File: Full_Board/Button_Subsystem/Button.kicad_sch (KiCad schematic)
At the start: 6 parts

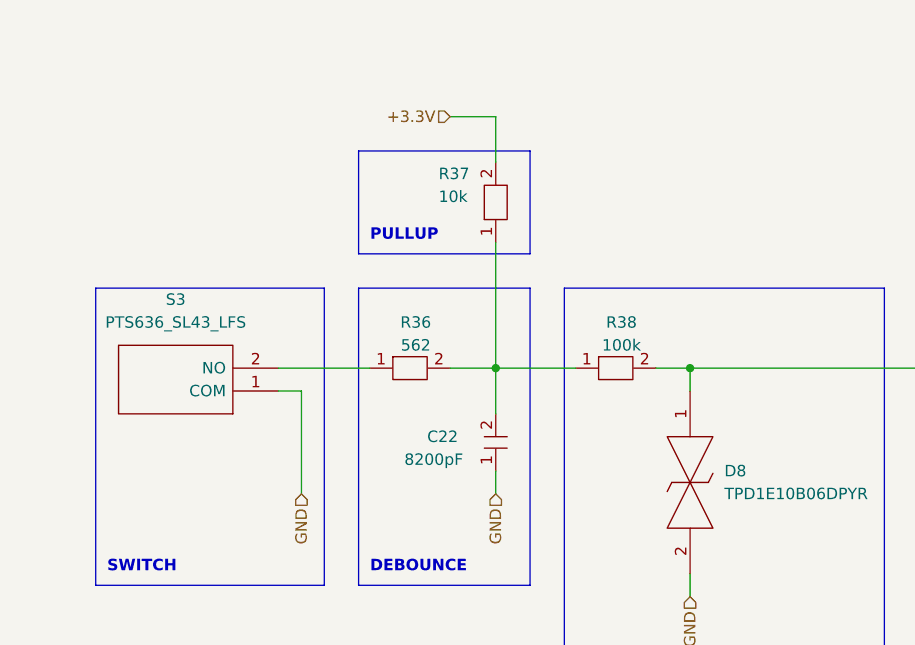
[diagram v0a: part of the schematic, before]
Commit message: Added 5V power supply
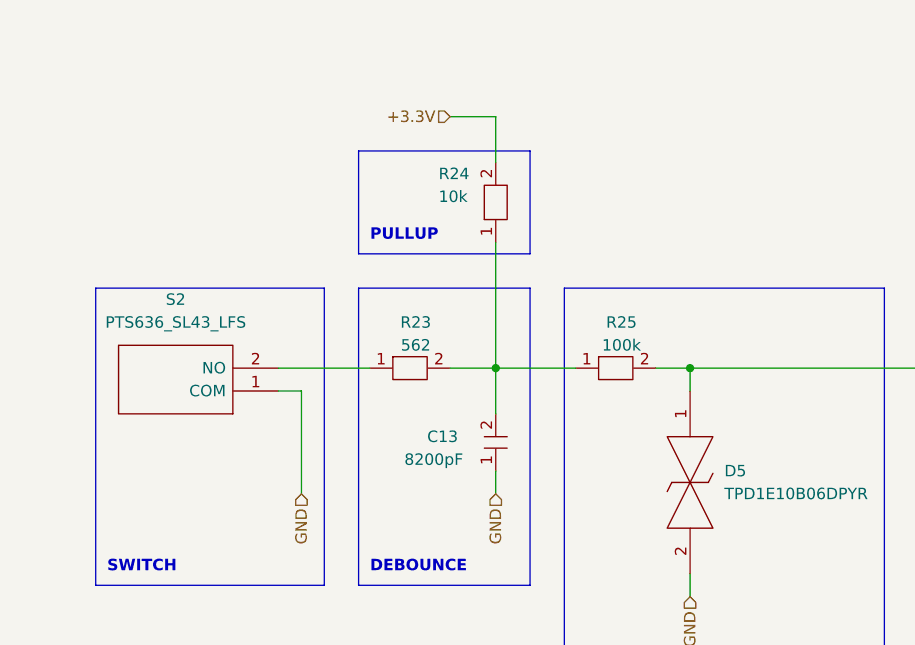
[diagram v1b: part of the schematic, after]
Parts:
- renumbered C22 to C13, D8 to D5, R36 to R23, R37 to R24, R38 to R25, S3 to S2
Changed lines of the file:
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@@
     (effects (font (size 1.27 1.27)) (justify right))
   )
-  (symbol (lib_id "CR0402-FX-5620GLF:CR0402-FX-5620GLF") (at 123.19 96.52 0) (unit 1)
+  (symbol (lib_id "CR0402-FX-5620GLF:CR0402-FX-5620GLF") (at 123.19 96.52 0)
     (in_bom yes) (on_board yes)
-    (property "Reference" "R36" (id 0) (at 128.27 91.44 0))
+    (property "Reference" "R23" (id 0) (at 128.27 91.44 0))
     (property "Value" "562" (id 1) (at 128.27 93.98 0))
     (property "Footprint" "CR0402-FX-5620GLF:RESC1005X40N" (id 2) (at 137.16 95.25 0)
@@
     (pin "2")
   )
-  (symbol (lib_id "TPD1E10B06DPYR:TPD1E10B06DPYR") (at 158.75 99.06 270) (unit 1)
+  (symbol (lib_id "TPD1E10B06DPYR:TPD1E10B06DPYR") (at 158.75 99.06 270)
     (in_bom yes) (on_board yes)
-    (property "Reference" "D8" (id 0) (at 162.56 107.95 90)
+    (property "Reference" "D5" (id 0) (at 162.56 107.95 90)
       (effects (font (size 1.27 1.27)) (justify left))
     )
@@
     (pin "2")
   )
-  (symbol (lib_id "RCV2512100KFKEGAT:RCV2512100KFKEGAT") (at 146.05 96.52 0) (unit 1)
+  (symbol (lib_id "RCV2512100KFKEGAT:RCV2512100KFKEGAT") (at 146.05 96.52 0)
     (in_bom yes) (on_board yes)
-    (property "Reference" "R38" (id 0) (at 151.13 91.44 0))
+    (property "Reference" "R25" (id 0) (at 151.13 91.44 0))
     (property "Value" "100k" (id 1) (at 151.13 93.98 0))
     (property "Footprint" "RCV2512100KFKEGAT:RESC6332X70N" (id 2) (at 160.02 95.25 0)
@@
     (pin "2")
   )
-  (symbol (lib_id "CRMA1210AF10K0DKEF:10k") (at 137.16 82.55 90) (unit 1)
+  (symbol (lib_id "CRMA1210AF10K0DKEF:10k") (at 137.16 82.55 90)
     (in_bom yes) (on_board yes)
-    (property "Reference" "R37" (id 0) (at 130.81 74.93 90)
+    (property "Reference" "R24" (id 0) (at 130.81 74.93 90)
       (effects (font (size 1.27 1.27)) (justify right))
     )
@@
     (pin "2")
   )
-  (symbol (lib_id "PTS636_SL43_LFS:PTS636_SL43_LFS") (at 113.03 99.06 180) (unit 1)
+  (symbol (lib_id "PTS636_SL43_LFS:PTS636_SL43_LFS") (at 113.03 99.06 180)
     (in_bom yes) (on_board yes) (fields_autoplaced)
-    (property "Reference" "S3" (id 0) (at 101.6 88.9 0))
+    (property "Reference" "S2" (id 0) (at 101.6 88.9 0))
     (property "Value" "PTS636_SL43_LFS" (id 1) (at 101.6 91.44 0))
     (property "Footprint" "PTS636_SL43_LFS:PTS636SL43LFS" (id 2) (at 93.98 101.6 0)
@@
     (pin "2")
   )
-  (symbol (lib_id "C1210C822K2RACAUTO:8200pF") (at 137.16 107.95 90) (unit 1)
+  (symbol (lib_id "C1210C822K2RACAUTO:8200pF") (at 137.16 107.95 90)
     (in_bom yes) (on_board yes)
-    (property "Reference" "C22" (id 0) (at 129.54 104.14 90)
+    (property "Reference" "C13" (id 0) (at 129.54 104.14 90)
       (effects (font (size 1.27 1.27)) (justify right))
     )

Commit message: Added extra bypass caps to the power supply
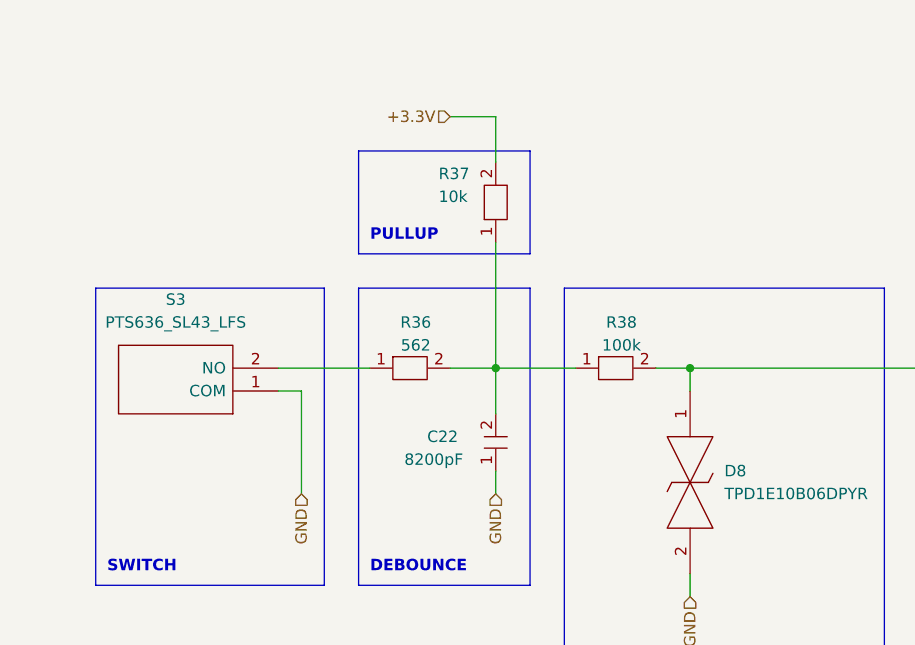
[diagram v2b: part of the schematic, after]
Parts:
- renumbered C13 to C22, D5 to D8, R23 to R36, R24 to R37, R25 to R38, S2 to S3
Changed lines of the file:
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@@
   (symbol (lib_id "CR0402-FX-5620GLF:CR0402-FX-5620GLF") (at 123.19 96.52 0)
     (in_bom yes) (on_board yes)
-    (property "Reference" "R23" (id 0) (at 128.27 91.44 0))
+    (property "Reference" "R36" (id 0) (at 128.27 91.44 0))
     (property "Value" "562" (id 1) (at 128.27 93.98 0))
     (property "Footprint" "CR0402-FX-5620GLF:RESC1005X40N" (id 2) (at 137.16 95.25 0)
@@
   (symbol (lib_id "TPD1E10B06DPYR:TPD1E10B06DPYR") (at 158.75 99.06 270)
     (in_bom yes) (on_board yes)
-    (property "Reference" "D5" (id 0) (at 162.56 107.95 90)
+    (property "Reference" "D8" (id 0) (at 162.56 107.95 90)
       (effects (font (size 1.27 1.27)) (justify left))
     )
@@
   (symbol (lib_id "RCV2512100KFKEGAT:RCV2512100KFKEGAT") (at 146.05 96.52 0)
     (in_bom yes) (on_board yes)
-    (property "Reference" "R25" (id 0) (at 151.13 91.44 0))
+    (property "Reference" "R38" (id 0) (at 151.13 91.44 0))
     (property "Value" "100k" (id 1) (at 151.13 93.98 0))
     (property "Footprint" "RCV2512100KFKEGAT:RESC6332X70N" (id 2) (at 160.02 95.25 0)
@@
   (symbol (lib_id "CRMA1210AF10K0DKEF:10k") (at 137.16 82.55 90)
     (in_bom yes) (on_board yes)
-    (property "Reference" "R24" (id 0) (at 130.81 74.93 90)
+    (property "Reference" "R37" (id 0) (at 130.81 74.93 90)
       (effects (font (size 1.27 1.27)) (justify right))
     )
@@
   (symbol (lib_id "PTS636_SL43_LFS:PTS636_SL43_LFS") (at 113.03 99.06 180)
     (in_bom yes) (on_board yes) (fields_autoplaced)
-    (property "Reference" "S2" (id 0) (at 101.6 88.9 0))
+    (property "Reference" "S3" (id 0) (at 101.6 88.9 0))
     (property "Value" "PTS636_SL43_LFS" (id 1) (at 101.6 91.44 0))
     (property "Footprint" "PTS636_SL43_LFS:PTS636SL43LFS" (id 2) (at 93.98 101.6 0)
@@
   (symbol (lib_id "C1210C822K2RACAUTO:8200pF") (at 137.16 107.95 90)
     (in_bom yes) (on_board yes)
-    (property "Reference" "C13" (id 0) (at 129.54 104.14 90)
+    (property "Reference" "C22" (id 0) (at 129.54 104.14 90)
       (effects (font (size 1.27 1.27)) (justify right))
     )

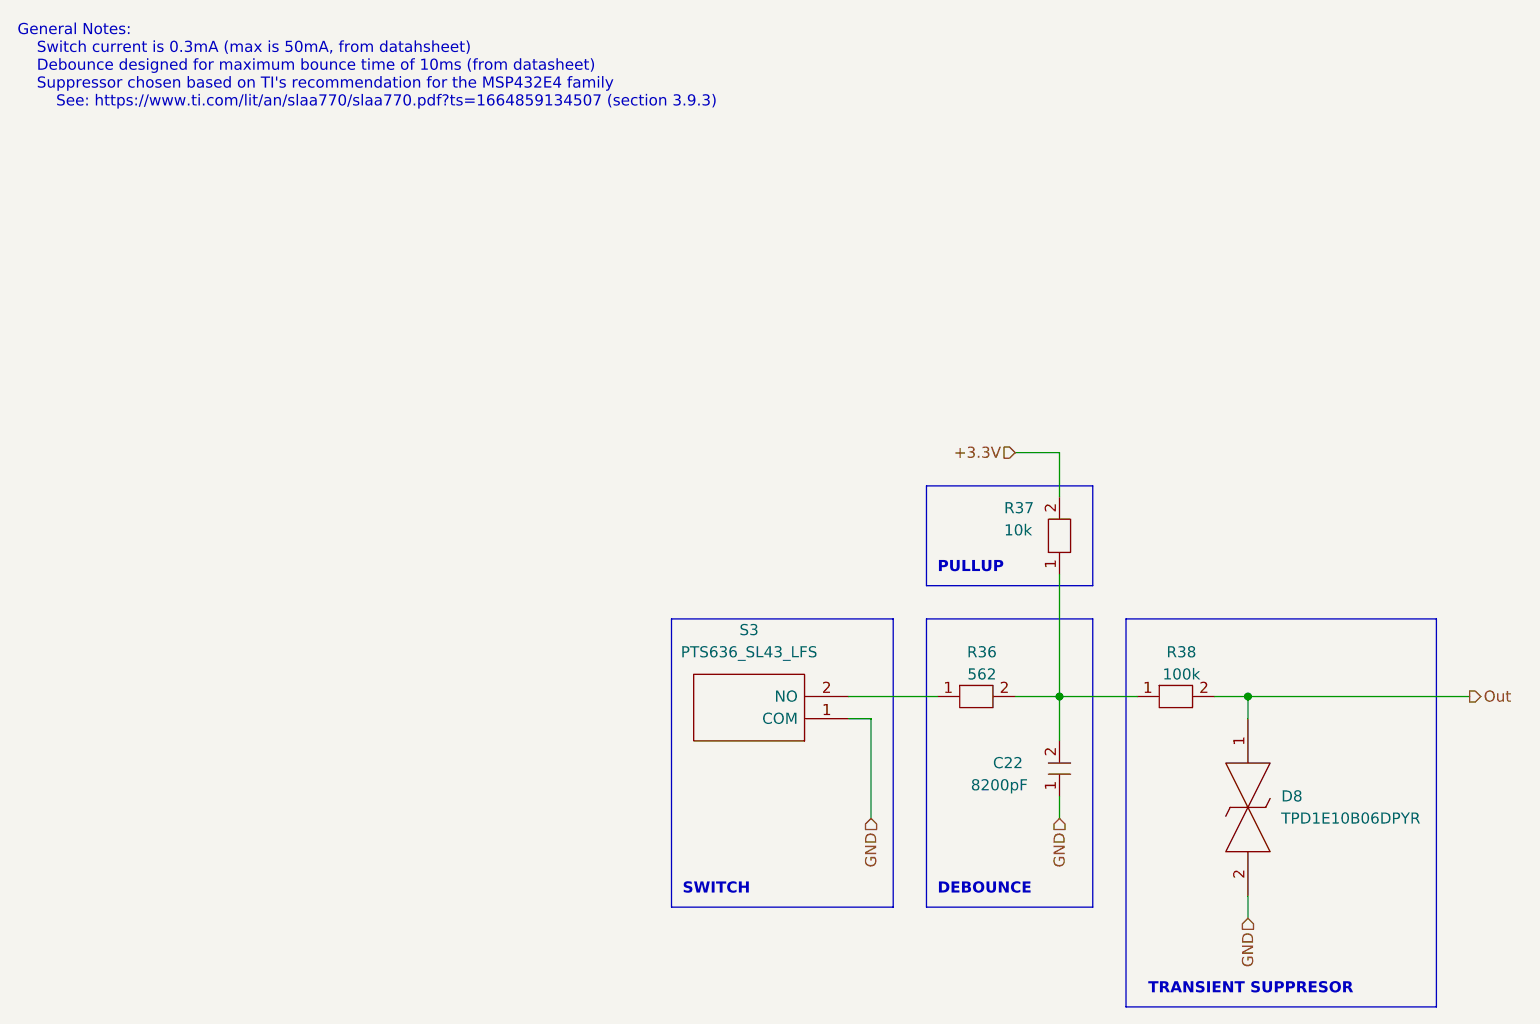
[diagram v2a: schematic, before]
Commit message: Merge Eli and Gabi files. Remove unecessary ECAD remnants. Update stepper components post-part order
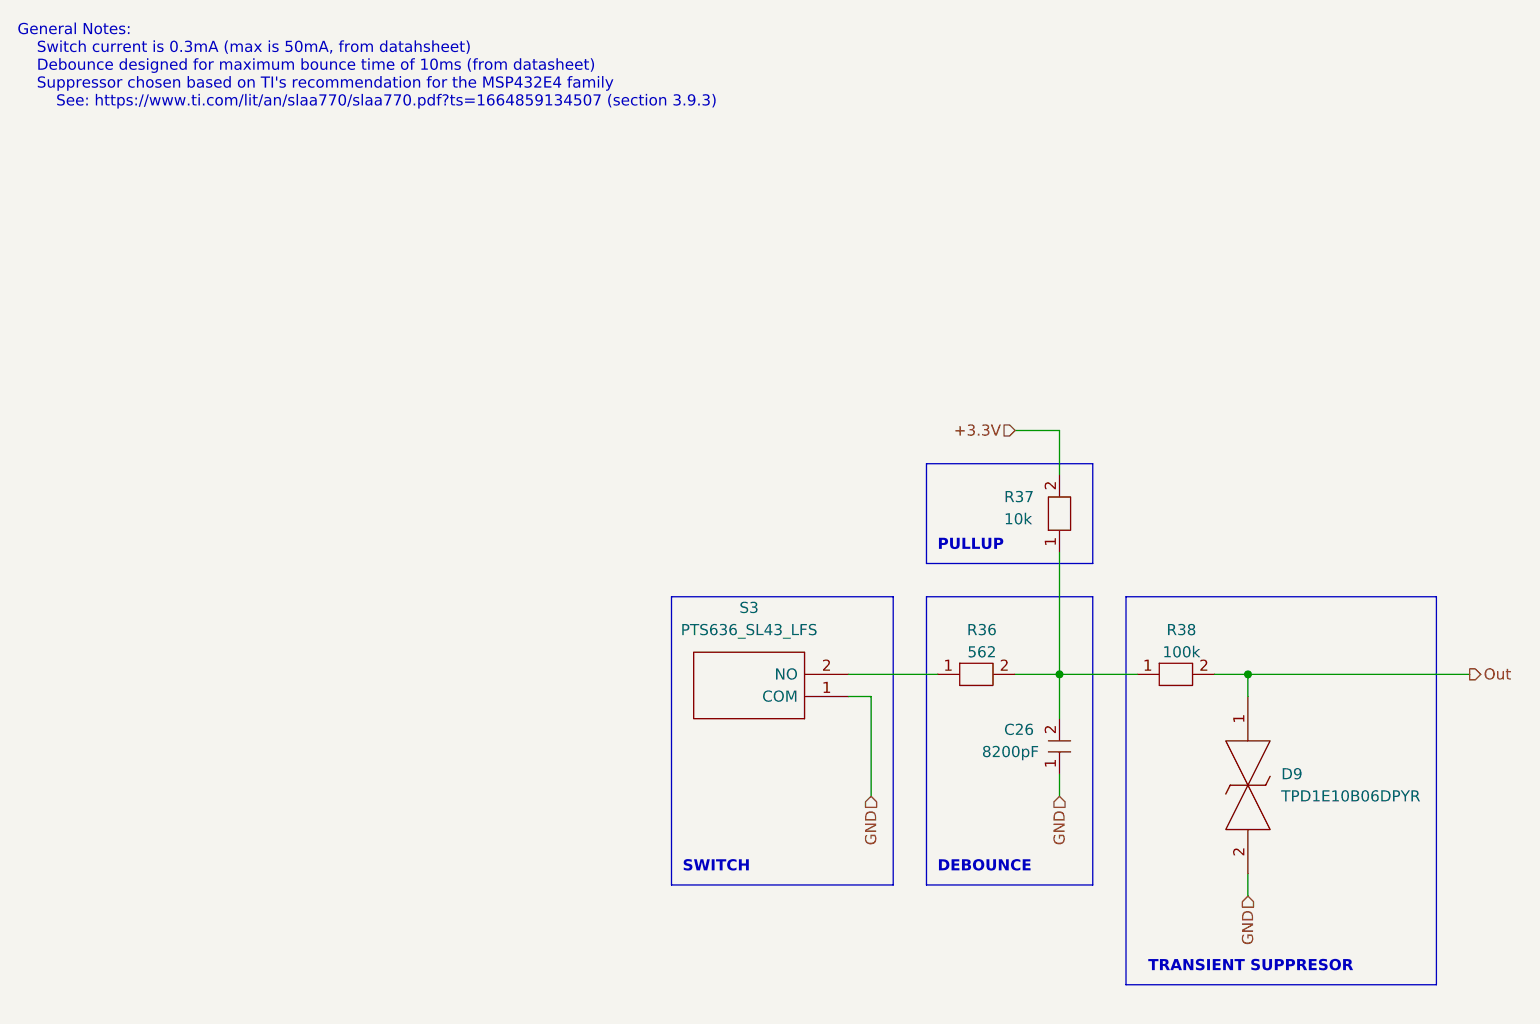
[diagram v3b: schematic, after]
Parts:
- removed C22: 8200pF, C1210C822K2RACAUTO:CAPC3225X88N, symbol C1210C822K2RACAUTO:8200pF
- removed D8: TPD1E10B06DPYR, TPD1E10B06DPYR:TPD1E10B06DPYR, symbol TPD1E10B06DPYR:TPD1E10B06DPYR
- removed R37: 10k, CRMA1210AF10K0DKEF:RESC3225X74N, symbol CRMA1210AF10K0DKEF:10k
- added C26: 8200pF, C1210C822K2RACAUTO:CAPC3225X88N, symbol C1210C822K2RACAUTO:C1210C822K2RACAUTO
- added D9: TPD1E10B06DPYR, TPD1E10B06DPYR:TPD1E10B06DPYR, symbol TPD1E10B06DPYR:TPD1E10B06DPYR
- added R37: 10k, RESC3225X74N, symbol RMCF1206FT10K0:10k
- R36: Mouse link (none) -> https://www.mouser.com/ProductDetail/Bourns/CR0402-FX-5620G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; Mouser link https://www.mouser.com/ProductDetail/Bourns/CR0402-FX-5620G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 -> (none)
- S3: Mouser link  (none) -> https://www.mouser.com/ProductDetail/CK/PTS636-SL43-LFS?qs=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
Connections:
- net +3.3V: now also R37.2
- net GND: now also C26.1, D9.2
- net Out: now also D9.1
- net at R36.2, R38.1: now also C26.2, R37.1

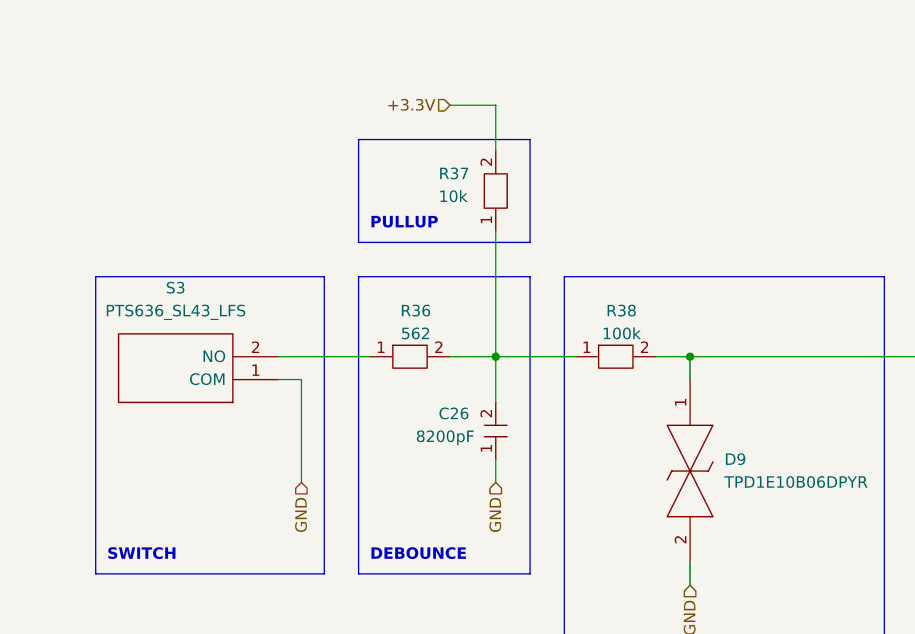
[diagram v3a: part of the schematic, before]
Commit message: Added a fuse and fixed ERC
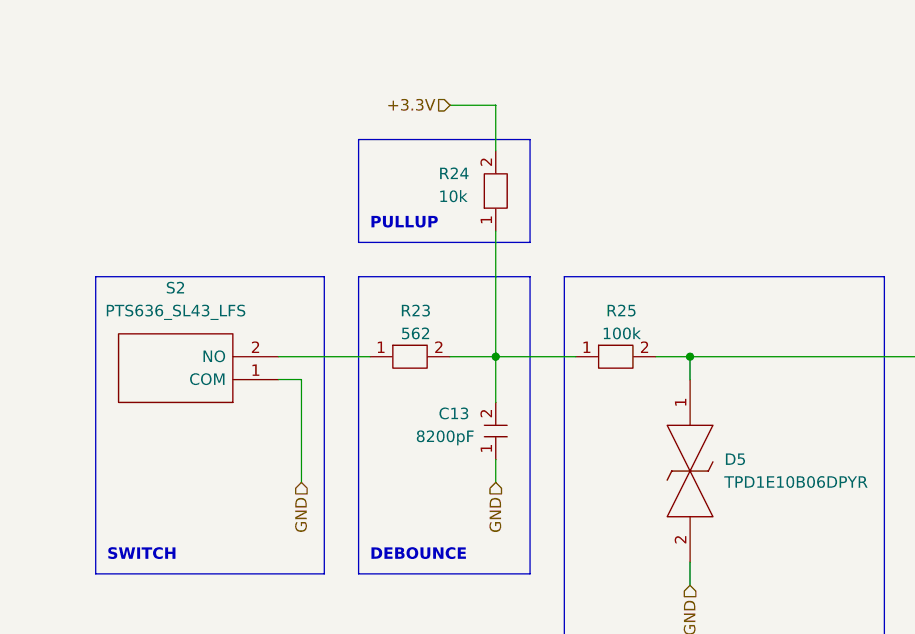
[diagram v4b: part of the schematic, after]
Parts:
- renumbered C26 to C13, D9 to D5, R36 to R23, R37 to R24, R38 to R25, S3 to S2
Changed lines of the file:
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@@
     (effects (font (size 1.27 1.27)) (justify right))
   )
-  (symbol (lib_id "RMCF1206FT10K0:10k") (at 137.16 80.01 90) (unit 1)
+  (symbol (lib_id "RMCF1206FT10K0:10k") (at 137.16 80.01 90)
     (in_bom yes) (on_board yes)
-    (property "Reference" "R37" (id 0) (at 130.81 73.66 90)
+    (property "Reference" "R24" (id 0) (at 130.81 73.66 90)
       (effects (font (size 1.27 1.27)) (justify right))
     )
@@
     (pin "2")
   )
-  (symbol (lib_id "C1210C822K2RACAUTO:C1210C822K2RACAUTO") (at 137.16 105.41 90) (unit 1)
+  (symbol (lib_id "C1210C822K2RACAUTO:C1210C822K2RACAUTO") (at 137.16 105.41 90)
     (in_bom yes) (on_board yes)
-    (property "Reference" "C26" (id 0) (at 130.81 100.33 90)
+    (property "Reference" "C13" (id 0) (at 130.81 100.33 90)
       (effects (font (size 1.27 1.27)) (justify right))
     )
@@
     (pin "2")
   )
-  (symbol (lib_id "CR0402-FX-5620GLF:CR0402-FX-5620GLF") (at 123.19 93.98 0) (unit 1)
+  (symbol (lib_id "CR0402-FX-5620GLF:CR0402-FX-5620GLF") (at 123.19 93.98 0)
     (in_bom yes) (on_board yes)
-    (property "Reference" "R36" (id 0) (at 128.27 88.9 0))
+    (property "Reference" "R23" (id 0) (at 128.27 88.9 0))
     (property "Value" "562" (id 1) (at 128.27 91.44 0))
     (property "Footprint" "CR0402-FX-5620GLF:RESC1005X40N" (id 2) (at 137.16 92.71 0)
@@
     (pin "2")
   )
-  (symbol (lib_id "RCV2512100KFKEGAT:RCV2512100KFKEGAT") (at 146.05 93.98 0) (unit 1)
+  (symbol (lib_id "RCV2512100KFKEGAT:RCV2512100KFKEGAT") (at 146.05 93.98 0)
     (in_bom yes) (on_board yes)
-    (property "Reference" "R38" (id 0) (at 151.13 88.9 0))
+    (property "Reference" "R25" (id 0) (at 151.13 88.9 0))
     (property "Value" "100k" (id 1) (at 151.13 91.44 0))
     (property "Footprint" "RCV2512100KFKEGAT:RESC6332X70N" (id 2) (at 160.02 92.71 0)
@@
     (pin "2")
   )
-  (symbol (lib_id "PTS636_SL43_LFS:PTS636_SL43_LFS") (at 113.03 96.52 180) (unit 1)
+  (symbol (lib_id "PTS636_SL43_LFS:PTS636_SL43_LFS") (at 113.03 96.52 180)
     (in_bom yes) (on_board yes) (fields_autoplaced)
-    (property "Reference" "S3" (id 0) (at 101.6 86.36 0))
+    (property "Reference" "S2" (id 0) (at 101.6 86.36 0))
     (property "Value" "PTS636_SL43_LFS" (id 1) (at 101.6 88.9 0))
     (property "Footprint" "PTS636_SL43_LFS:PTS636SL43LFS" (id 2) (at 93.98 99.06 0)
@@
     (pin "2")
   )
-  (symbol (lib_id "TPD1E10B06DPYR:TPD1E10B06DPYR") (at 158.75 96.52 270) (unit 1)
+  (symbol (lib_id "TPD1E10B06DPYR:TPD1E10B06DPYR") (at 158.75 96.52 270)
     (in_bom yes) (on_board yes)
-    (property "Reference" "D9" (id 0) (at 162.56 105.41 90)
+    (property "Reference" "D5" (id 0) (at 162.56 105.41 90)
       (effects (font (size 1.27 1.27)) (justify left))
     )
